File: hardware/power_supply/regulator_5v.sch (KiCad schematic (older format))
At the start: 45 parts

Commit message: Update: almost finished power supply schematic (incl. +24V)
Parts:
- removed Q?: IRLZ44N, symbol IRLZ44N
- removed T?: THYRISTOR, symbol THYRISTOR
- added D?: BT152-600R, symbol SCR-KAG
- added Q?: IRLZ44N, symbol MOS_N_IRF
- R?: value 3.3k 1% -> 3.0k 1%
- R?: value 2.2k 1% -> 2.0k 1%
- R?: value 100 -> 82
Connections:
- net GND: now also D?.1 (K)
- net +5_VRECT: now reaches C?.1, C?.1, D?.2 (K), D?.2 (K), F?.1, R?.1
- net +5_VFUSED: now reaches D?.1 (A), D?.1 (A), F?.2
- net +5_VFUSED: now also D?.2 (A), Q?.2 (D)
- net +5_VGATE: now reaches C?.1, C?.1, D?.2 (K), D?.2 (K), R?.1, R?.2
- net at C?.1, D?.2 (K), Q?.1 (C)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: now also Q?.1 (G)
- net at D?.1 (A), R?.2, R?.2: now also Q?.3 (S)
- net at R?.1, R?.2: now also D?.3 (G)
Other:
- note added: "On heatsink"
- note added: "Overvoltage protection circuit\nSetting: approx. 6.25V (min. 6.0V)\nAction: crowbar"
- note removed: "HS mounted"
- note removed: "Overvoltage protection\nSetting: approx. 6.25V\nAction: crowbar"
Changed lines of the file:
@@
 LIBS:contrib
 LIBS:valves
-LIBS:irlz44n
 LIBS:tl431
 LIBS:r_pot
+LIBS:mos_irf
+LIBS:scr
+LIBS:conn_mf
 LIBS:power_supply-cache
 EELAYER 24 0
@@
 $Descr A4 11693 8268
 encoding utf-8
-Sheet 2 3
-Title "+5V 2.0A voltage regulator"
+Sheet 2 4
+Title "+5V 2.0A digital supply regulator"
 Date "06 марта 2014"
 Rev ""
@@
 $EndComp
 $Comp
-L IRLZ44N Q?
-U 1 1 5317C141
-P 6050 3450
-F 0 "Q?" H 6300 3500 40  0000 L CNN
-F 1 "IRLZ44N" H 6300 3400 40  0000 L CNN
-F 2 "" H 5871 3551 29  0001 C CNN
-F 3 "" H 6050 3450 60  0000 C CNN
-	1    6050 3450
-	0    -1   -1   0
-$EndComp
-$Comp
 L R R?
 U 1 1 5317C19B
@@
 	6550 2650 6550 2600
 $Comp
-L THYRISTOR T?
-U 1 1 5318E06D
-P 4300 5950
-F 0 "T?" H 4200 6050 40  0000 C CNN
-F 1 "THYRISTOR" H 4300 5850 40  0000 C CNN
-F 2 "" H 4300 5950 60  0000 C CNN
-F 3 "" H 4300 5950 60  0000 C CNN
-	1    4300 5950
-	0    -1   1    0
-$EndComp
-$Comp
 L FUSE F?
 U 1 1 5318E2EE
@@
 P 8650 4000
 F 0 "R?" V 8730 4000 40  0000 C CNN
-F 1 "3.3k 1%" V 8657 4001 40  0000 C CNN
+F 1 "3.0k 1%" V 8657 4001 40  0000 C CNN
 F 2 "" V 8580 4000 30  0000 C CNN
 F 3 "" H 8650 4000 30  0000 C CNN
@@
 P 8650 5300
 F 0 "R?" V 8730 5300 40  0000 C CNN
-F 1 "2.2k 1%" V 8657 5301 40  0000 C CNN
+F 1 "2.0k 1%" V 8657 5301 40  0000 C CNN
 F 2 "" V 8580 5300 30  0000 C CNN
 F 3 "" H 8650 5300 30  0000 C CNN
@@
 P 9900 4500
 F 0 "R?" V 9980 4500 40  0000 C CNN
-F 1 "100" V 9907 4501 40  0000 C CNN
+F 1 "82" V 9907 4501 40  0000 C CNN
 F 2 "" V 9830 4500 30  0000 C CNN
 F 3 "" H 9900 4500 30  0000 C CNN
@@
 	4750 5850 4750 6050
 Wire Wire Line
-	4750 5950 5600 5950
+	4750 5950 5750 5950
 Wire Wire Line
 	1900 5100 1900 5250
@@
 	3100 3350 3100 3850
 Wire Wire Line
-	3400 3350 3400 3900
+	3400 3200 3400 3900
 Wire Wire Line
 	3100 4350 3100 4800
@@
 	4750 3350 4750 4750
 Wire Wire Line
-	4300 5750 4300 3350
+	4300 3200 4300 5750
 Connection ~ 4300 3350
 Wire Wire Line
@@
 Wire Notes Line
 	10050 6000 10050 5950
-Text Notes 8800 6300 0    60   ~ 0
-Overvoltage protection\nSetting: approx. 6.25V\nAction: crowbar
+Text Notes 8500 6300 0    60   ~ 0
+Overvoltage protection circuit\nSetting: approx. 6.25V (min. 6.0V)\nAction: crowbar
 Wire Notes Line
 	4600 6900 4600 6950
@@
 Text Notes 3900 7100 0    60   ~ 0
 SCR crowbar
-Wire Notes Line
-	4100 5700 4100 6200
-Wire Notes Line
-	4100 6200 4500 6200
-Wire Notes Line
-	4500 6200 4500 5700
-Wire Notes Line
-	4500 5700 4100 5700
-Text Notes 3650 5650 0    60   ~ 0
-HS mounted
-Wire Notes Line
-	5800 2900 6300 2900
-Wire Notes Line
-	6300 2900 6300 3700
-Wire Notes Line
-	6300 3700 5800 3700
-Wire Notes Line
-	5800 3700 5800 2900
-Text Notes 5800 2850 0    60   ~ 0
-HS mounted
+Text Notes 4150 6000 1    60   ~ 0
+On heatsink
 Text Notes 6250 2350 0    39   ~ 0
 Not fitted
@@
 	1    0    0    -1
 $EndComp
+$Comp
+L MOS_N_IRF Q?
+U 1 1 5324DDAD
+P 6050 3450
+F 0 "Q?" V 6400 3300 40  0000 L CNN
+F 1 "IRLZ44N" V 6300 3300 40  0000 L CNN
+F 2 "" H 5871 3551 29  0001 C CNN
+F 3 "" H 6050 3450 60  0000 C CNN
+	1    6050 3450
+	0    -1   -1   0
+$EndComp
+$Comp
+L SCR-KAG D?
+U 1 1 5324EEC7
+P 4300 5950
+F 0 "D?" H 4200 6050 40  0000 C CNN
+F 1 "BT152-600R" H 4300 5850 40  0000 C CNN
+F 2 "" H 4300 5950 60  0000 C CNN
+F 3 "" H 4300 5950 60  0000 C CNN
+	1    4300 5950
+	0    -1   1    0
+$EndComp
+Text Label 5750 5950 0    60   ~ 0
++5_VGATE
+Text Label 3400 3200 1    60   ~ 0
++5_VRECT
+Text Label 4300 3200 1    60   ~ 0
++5_VFUSED
+Text Notes 6200 3050 2    60   ~ 0
+On heatsink
 $EndSCHEMATC

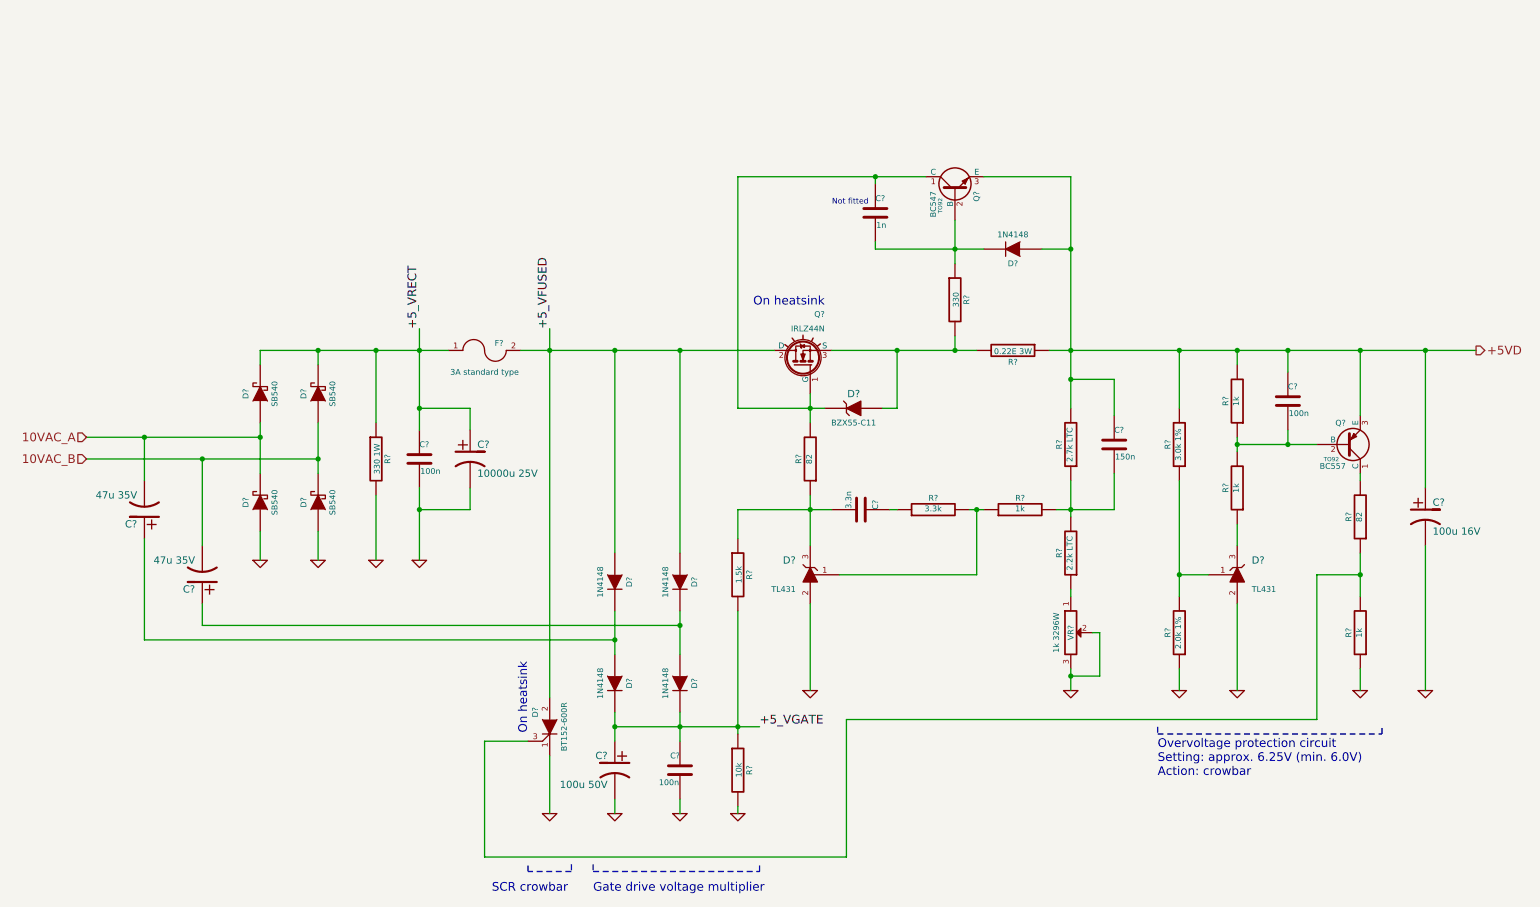
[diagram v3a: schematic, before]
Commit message: Update: PCB, schematic fixes -Almost completed power supply PCB -Removed discharge resistors from +-15, +24V supplies: no place on PCB for them -Removed ceramic capacitors (stayed in parallel with electrolytic caps): no reason for them
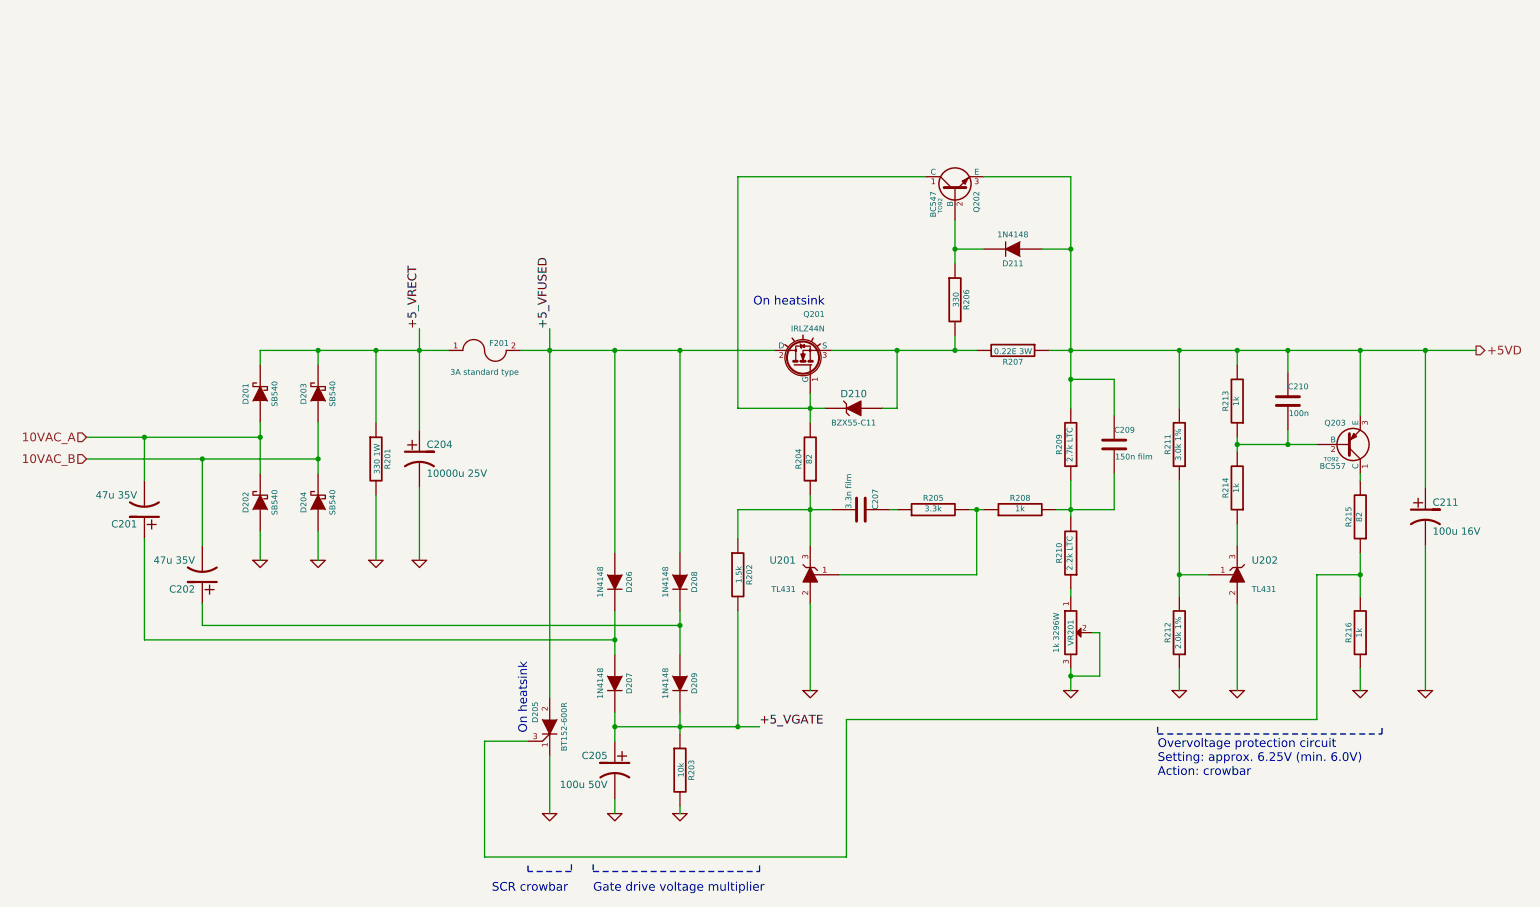
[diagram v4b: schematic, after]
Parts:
- removed C? (x2): 100n, symbol C
- removed C?: 1n, symbol C
- removed D? (x2): TL431, TO92, symbol TL431
- added U201, U202: TL431, TO92, symbol TL431
- C207: renamed from C?; value 3.3n -> 3.3n film
- C209: renamed from C?; value 150n -> 150n film
- gave numbers to parts that had none: 38
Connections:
- net GND: now also U201.2 (A), U202.2 (A)
- net at C207.2, R202.1, R204.1: now also U201.3 (K)
- net at R205.2, R208.1: now also U201.1 (Ref)
- net at R211.1, R212.2: now also U202.1 (Ref)
- net at R214.1: now also U202.3 (K)
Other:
- note removed: "Not fitted"
- moved on the sheet: C204, R203
